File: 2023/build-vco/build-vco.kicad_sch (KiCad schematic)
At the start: 1 part, among them M27 NMOS_OR1

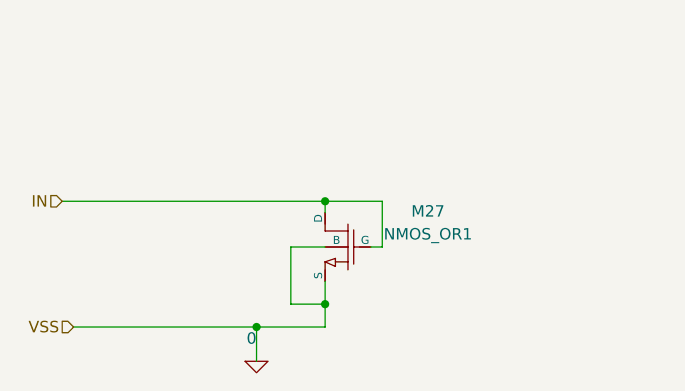
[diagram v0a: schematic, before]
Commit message: PMOS x1 NMOS x 2 まで成長させた。
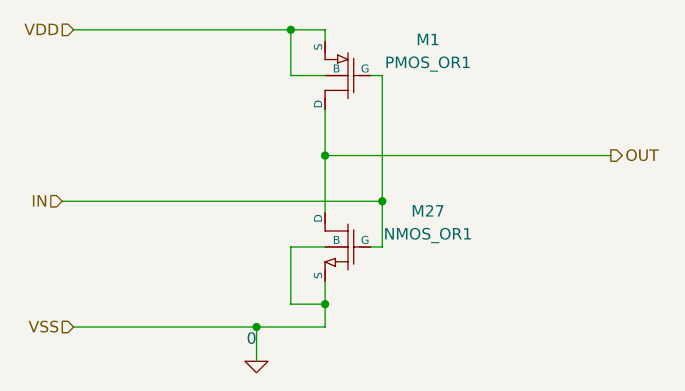
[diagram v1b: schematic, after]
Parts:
- added M1: PMOS_OR1, symbol OR1Symbols:PMOS_OR1
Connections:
- net IN: now also M1.2 (G); no longer M27.1 (D)
- new net OUT: M1.1 (D), M27.1 (D)
- new net VDD: M1.3 (S), M1.4 (B)
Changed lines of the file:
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@@
 (kicad_sch (version 20230121) (generator eeschema)
   (paper "A4")
-  (junction (at 132.08 73.66) (diameter 0) (color 0 0 0 0)
+  (junction (at 132.08 68.58) (diameter 0) (color 0 0 0 0)
+  )
+  (junction (at 138.43 73.66) (diameter 0) (color 0 0 0 0)
   )
   (junction (at 132.08 85.09) (diameter 0) (color 0 0 0 0)
   )
+  (junction (at 128.27 54.61) (diameter 0) (color 0 0 0 0)
+  )
   (junction (at 124.46 87.63) (diameter 0) (color 0 0 0 0)
   )
+  (wire (pts (xy 104.14 54.61) (xy 128.27 54.61))
+    (stroke (width 0) (type default))
+  )
+  (wire (pts (xy 132.08 54.61) (xy 132.08 55.88))
+    (stroke (width 0) (type default))
+  )
   (wire (pts (xy 104.14 87.63) (xy 124.46 87.63))
     (stroke (width 0) (type default))
   )
-  (wire (pts (xy 102.87 73.66) (xy 132.08 73.66))
-    (stroke (width 0) (type default))
-  )
-  (wire (pts (xy 132.08 73.66) (xy 132.08 74.93))
+  (wire (pts (xy 102.87 73.66) (xy 138.43 73.66))
+    (stroke (width 0) (type default))
+  )
+  (wire (pts (xy 137.16 59.69) (xy 138.43 59.69))
     (stroke (width 0) (type default))
   )
@@
     (stroke (width 0) (type default))
   )
-  (wire (pts (xy 132.08 73.66) (xy 138.43 73.66))
-    (stroke (width 0) (type default))
-  )
   (wire (pts (xy 124.46 87.63) (xy 124.46 91.44))
     (stroke (width 0) (type default))
@@
     (stroke (width 0) (type default))
   )
+  (wire (pts (xy 138.43 59.69) (xy 138.43 73.66))
+    (stroke (width 0) (type default))
+  )
+  (wire (pts (xy 132.08 68.58) (xy 163.83 68.58))
+    (stroke (width 0) (type default))
+  )
   (wire (pts (xy 128.27 78.74) (xy 128.27 85.09))
     (stroke (width 0) (type default))
@@
     (stroke (width 0) (type default))
   )
+  (wire (pts (xy 128.27 59.69) (xy 128.27 54.61))
+    (stroke (width 0) (type default))
+  )
+  (wire (pts (xy 132.08 59.69) (xy 128.27 59.69))
+    (stroke (width 0) (type default))
+  )
+  (wire (pts (xy 128.27 54.61) (xy 132.08 54.61))
+    (stroke (width 0) (type default))
+  )
   (wire (pts (xy 132.08 82.55) (xy 132.08 85.09))
     (stroke (width 0) (type default))
@@
   (wire (pts (xy 132.08 85.09) (xy 132.08 87.63))
     (stroke (width 0) (type default))
+  )
+  (wire (pts (xy 132.08 68.58) (xy 132.08 74.93))
+    (stroke (width 0) (type default))
+  )
+  (wire (pts (xy 132.08 63.5) (xy 132.08 68.58))
+    (stroke (width 0) (type default))
+  )
+  (hierarchical_label "VDD" (shape input) (at 104.14 54.61 180) (fields_autoplaced)
+    (effects (font (size 1.27 1.27)) (justify right))
   )
   (hierarchical_label "VSS" (shape input) (at 104.14 87.63 180) (fields_autoplaced)
     (effects (font (size 1.27 1.27)) (justify right))
+  )
+  (hierarchical_label "OUT" (shape output) (at 163.83 68.58 0) (fields_autoplaced)
+    (effects (font (size 1.27 1.27)) (justify left))
   )
   (hierarchical_label "IN" (shape input) (at 102.87 73.66 180) (fields_autoplaced)
@@
     )
   )
+  (symbol (lib_id "OR1Symbols:PMOS_OR1") (at 137.16 59.69 0) (mirror y) (unit 1)
+    (in_bom yes) (on_board yes) (dnp no) (fields_autoplaced)
+    (property "Reference" "M1" (at 143.51 55.7277 0)
+      (effects (font (size 1.27 1.27)))
+    )
+    (property "Value" "PMOS_OR1" (at 143.51 58.2677 0)
+      (effects (font (size 1.27 1.27)))
+    )
+    (property "Footprint" "" (at 137.16 59.69 0)
+      (effects (font (size 1.27 1.27)) hide)
+    )
+    (property "Datasheet" "" (at 137.16 59.69 0)
+      (effects (font (size 1.27 1.27)) hide)
+    )
+    (property "Sim.Pins" "1=1 2=2 3=3 4=4" (at 137.16 59.69 0)
+      (effects (font (size 1.27 1.27)) hide)
+    )
+    (property "Sim.Device" "SPICE" (at 128.27 64.77 0)
+      (effects (font (size 1.27 1.27)) (justify left) hide)
+    )
+    (property "Sim.Params" "type=\"M\" model=\"PMOS_OR1 l=1u w=6u\" lib=\"\"" (at 137.16 59.69 0)
+      (effects (font (size 1.27 1.27)) hide)
+    )
+    (pin "1")
+    (pin "2")
+    (pin "3")
+    (pin "4")
+    (instances
+      (project "build-vco"
+        (path "/178e7a69-f569-4b69-ab89-e6b9cdb6309f"
+          (reference "M1") (unit 1)
+        )
+      )
+    )
+  )
   (symbol (lib_id "OR1Symbols:0") (at 124.46 91.44 0) (unit 1)
     (in_bom yes) (on_board yes) (dnp no) (fields_autoplaced)
@@
           (reference "#GND02") (unit 1)
         )
+      )
+      (project "build-vco"
+        (path "/178e7a69-f569-4b69-ab89-e6b9cdb6309f"
+          (reference "#GND02") (unit 1)
+        )

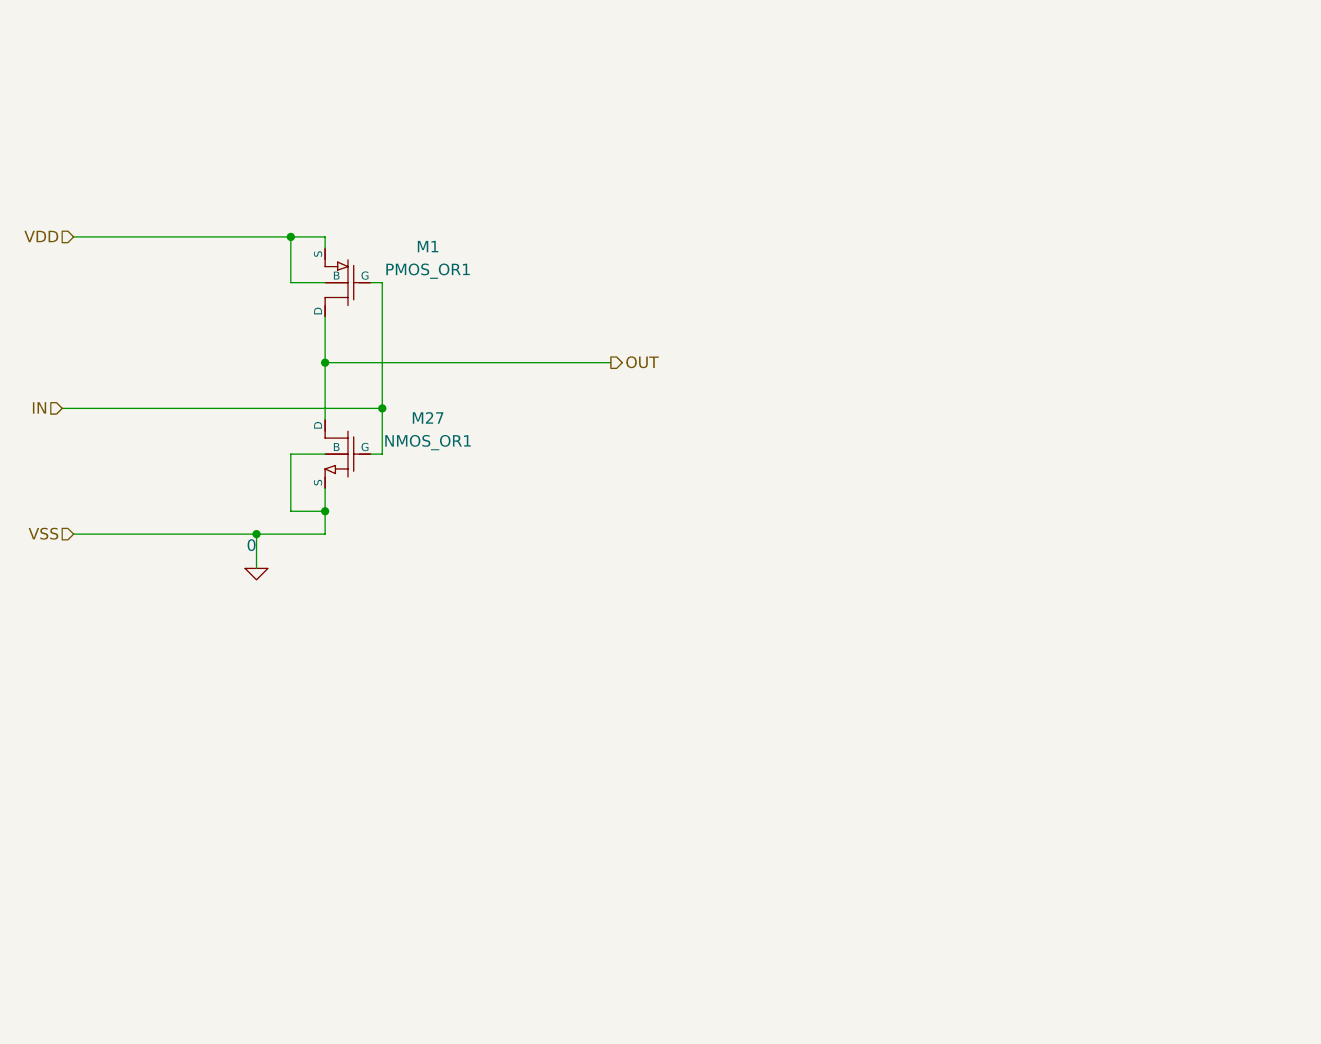
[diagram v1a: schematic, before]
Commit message: PMOS x 1, NMOS x1 に後退。しかし LVS は通る。
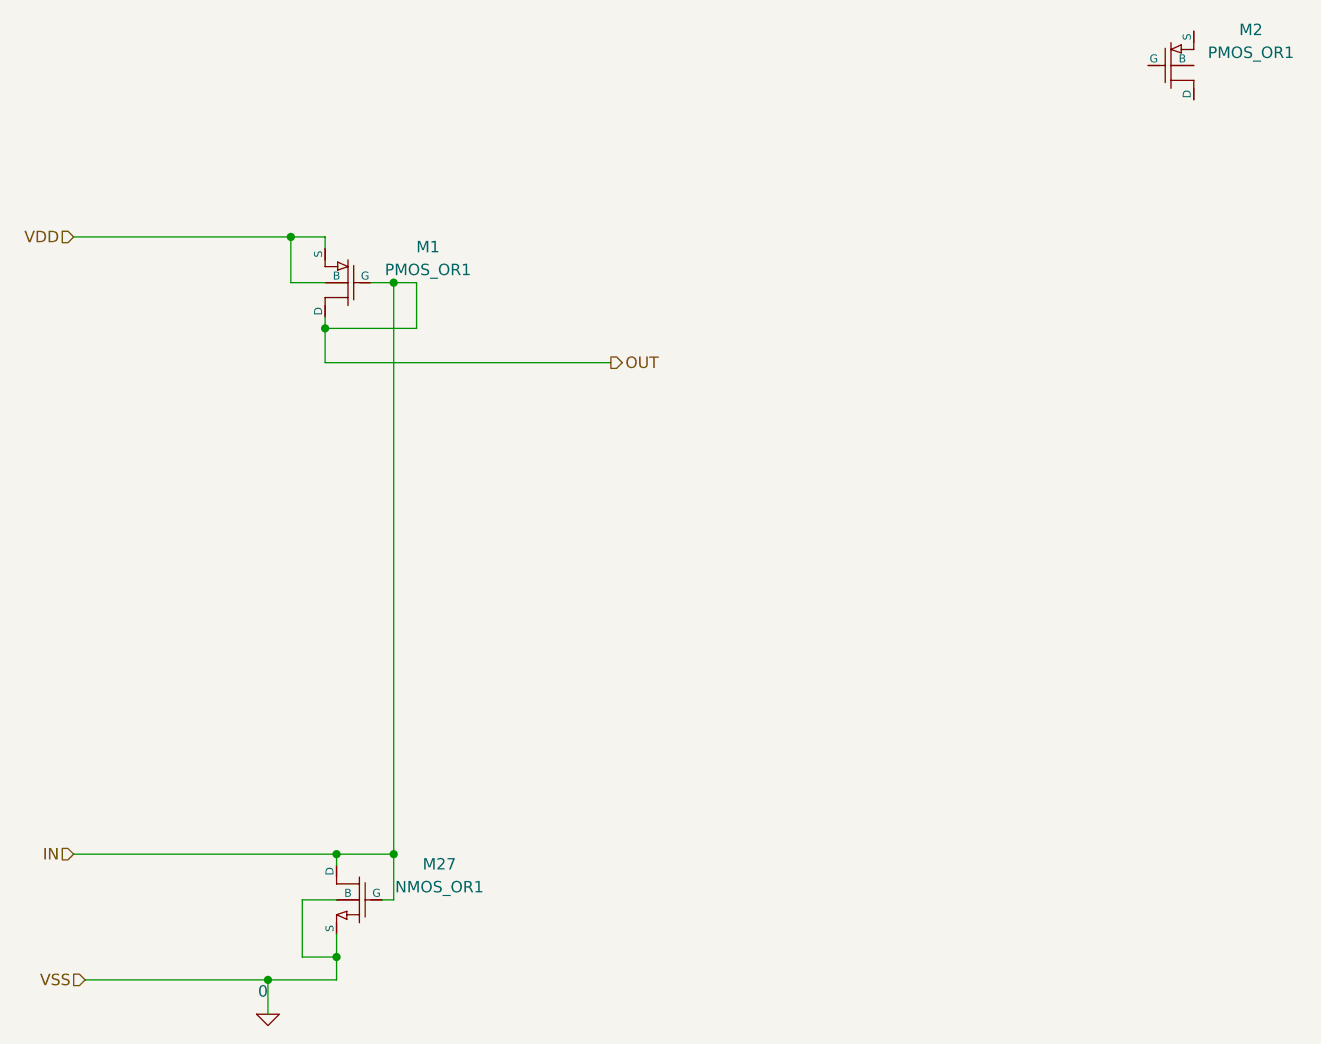
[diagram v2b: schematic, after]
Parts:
- added M2: PMOS_OR1, symbol OR1Symbols:PMOS_OR1
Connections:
- net OUT is gone; now on net IN: M1.1 (D), M27.1 (D)
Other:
- moved on the sheet: M27
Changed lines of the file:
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@@
 (kicad_sch (version 20230121) (generator eeschema)
   (paper "A4")
-  (junction (at 132.08 68.58) (diameter 0) (color 0 0 0 0)
-  )
-  (junction (at 138.43 73.66) (diameter 0) (color 0 0 0 0)
-  )
-  (junction (at 132.08 85.09) (diameter 0) (color 0 0 0 0)
+  (junction (at 133.35 123.19) (diameter 0) (color 0 0 0 0)
+  )
+  (junction (at 139.7 59.69) (diameter 0) (color 0 0 0 0)
+  )
+  (junction (at 139.7 123.19) (diameter 0) (color 0 0 0 0)
+  )
+  (junction (at 132.08 64.77) (diameter 0) (color 0 0 0 0)
+  )
+  (junction (at 133.35 134.62) (diameter 0) (color 0 0 0 0)
   )
   (junction (at 128.27 54.61) (diameter 0) (color 0 0 0 0)
   )
-  (junction (at 124.46 87.63) (diameter 0) (color 0 0 0 0)
+  (junction (at 125.73 137.16) (diameter 0) (color 0 0 0 0)
   )
   (wire (pts (xy 104.14 54.61) (xy 128.27 54.61))
@@
     (stroke (width 0) (type default))
   )
-  (wire (pts (xy 104.14 87.63) (xy 124.46 87.63))
-    (stroke (width 0) (type default))
-  )
-  (wire (pts (xy 102.87 73.66) (xy 138.43 73.66))
-    (stroke (width 0) (type default))
-  )
-  (wire (pts (xy 137.16 59.69) (xy 138.43 59.69))
-    (stroke (width 0) (type default))
-  )
-  (wire (pts (xy 138.43 73.66) (xy 138.43 78.74))
-    (stroke (width 0) (type default))
-  )
-  (wire (pts (xy 124.46 87.63) (xy 124.46 91.44))
-    (stroke (width 0) (type default))
-  )
-  (wire (pts (xy 132.08 78.74) (xy 128.27 78.74))
-    (stroke (width 0) (type default))
-  )
-  (wire (pts (xy 138.43 59.69) (xy 138.43 73.66))
+  (wire (pts (xy 105.41 137.16) (xy 125.73 137.16))
+    (stroke (width 0) (type default))
+  )
+  (wire (pts (xy 104.14 123.19) (xy 133.35 123.19))
+    (stroke (width 0) (type default))
+  )
+  (wire (pts (xy 139.7 123.19) (xy 139.7 128.27))
+    (stroke (width 0) (type default))
+  )
+  (wire (pts (xy 133.35 123.19) (xy 133.35 124.46))
+    (stroke (width 0) (type default))
+  )
+  (wire (pts (xy 125.73 137.16) (xy 125.73 140.97))
+    (stroke (width 0) (type default))
+  )
+  (wire (pts (xy 133.35 128.27) (xy 129.54 128.27))
+    (stroke (width 0) (type default))
+  )
+  (wire (pts (xy 139.7 59.69) (xy 139.7 123.19))
+    (stroke (width 0) (type default))
+  )
+  (wire (pts (xy 142.24 64.77) (xy 132.08 64.77))
+    (stroke (width 0) (type default))
+  )
+  (wire (pts (xy 129.54 128.27) (xy 129.54 134.62))
+    (stroke (width 0) (type default))
+  )
+  (wire (pts (xy 125.73 137.16) (xy 133.35 137.16))
+    (stroke (width 0) (type default))
+  )
+  (wire (pts (xy 138.43 128.27) (xy 139.7 128.27))
+    (stroke (width 0) (type default))
+  )
+  (wire (pts (xy 129.54 134.62) (xy 133.35 134.62))
+    (stroke (width 0) (type default))
+  )
+  (wire (pts (xy 137.16 59.69) (xy 139.7 59.69))
+    (stroke (width 0) (type default))
+  )
+  (wire (pts (xy 132.08 64.77) (xy 132.08 68.58))
+    (stroke (width 0) (type default))
+  )
+  (wire (pts (xy 128.27 59.69) (xy 128.27 54.61))
+    (stroke (width 0) (type default))
+  )
+  (wire (pts (xy 132.08 59.69) (xy 128.27 59.69))
+    (stroke (width 0) (type default))
+  )
+  (wire (pts (xy 128.27 54.61) (xy 132.08 54.61))
+    (stroke (width 0) (type default))
+  )
+  (wire (pts (xy 133.35 132.08) (xy 133.35 134.62))
+    (stroke (width 0) (type default))
+  )
+  (wire (pts (xy 139.7 59.69) (xy 142.24 59.69))
+    (stroke (width 0) (type default))
+  )
+  (wire (pts (xy 142.24 59.69) (xy 142.24 64.77))
+    (stroke (width 0) (type default))
+  )
+  (wire (pts (xy 133.35 123.19) (xy 139.7 123.19))
+    (stroke (width 0) (type default))
+  )
+  (wire (pts (xy 133.35 134.62) (xy 133.35 137.16))
     (stroke (width 0) (type default))
   )
@@
     (stroke (width 0) (type default))
   )
-  (wire (pts (xy 128.27 78.74) (xy 128.27 85.09))
-    (stroke (width 0) (type default))
-  )
-  (wire (pts (xy 124.46 87.63) (xy 132.08 87.63))
-    (stroke (width 0) (type default))
-  )
-  (wire (pts (xy 137.16 78.74) (xy 138.43 78.74))
-    (stroke (width 0) (type default))
-  )
-  (wire (pts (xy 128.27 85.09) (xy 132.08 85.09))
-    (stroke (width 0) (type default))
-  )
-  (wire (pts (xy 128.27 59.69) (xy 128.27 54.61))
-    (stroke (width 0) (type default))
-  )
-  (wire (pts (xy 132.08 59.69) (xy 128.27 59.69))
-    (stroke (width 0) (type default))
-  )
-  (wire (pts (xy 128.27 54.61) (xy 132.08 54.61))
-    (stroke (width 0) (type default))
-  )
-  (wire (pts (xy 132.08 82.55) (xy 132.08 85.09))
-    (stroke (width 0) (type default))
-  )
-  (wire (pts (xy 132.08 85.09) (xy 132.08 87.63))
-    (stroke (width 0) (type default))
-  )
-  (wire (pts (xy 132.08 68.58) (xy 132.08 74.93))
-    (stroke (width 0) (type default))
-  )
-  (wire (pts (xy 132.08 63.5) (xy 132.08 68.58))
+  (wire (pts (xy 132.08 63.5) (xy 132.08 64.77))
     (stroke (width 0) (type default))
   )
@@
     (effects (font (size 1.27 1.27)) (justify right))
   )
-  (hierarchical_label "VSS" (shape input) (at 104.14 87.63 180) (fields_autoplaced)
+  (hierarchical_label "VSS" (shape input) (at 105.41 137.16 180) (fields_autoplaced)
     (effects (font (size 1.27 1.27)) (justify right))
   )
@@
     (effects (font (size 1.27 1.27)) (justify left))
   )
-  (hierarchical_label "IN" (shape input) (at 102.87 73.66 180) (fields_autoplaced)
+  (hierarchical_label "IN" (shape input) (at 104.14 123.19 180) (fields_autoplaced)
     (effects (font (size 1.27 1.27)) (justify right))
   )
-  (symbol (lib_id "OR1Symbols:NMOS_OR1") (at 137.16 78.74 0) (mirror y) (unit 1)
-    (in_bom yes) (on_board yes) (dnp no) (fields_autoplaced)
-    (property "Reference" "M27" (at 143.51 74.7777 0)
-      (effects (font (size 1.27 1.27)))
-    )
-    (property "Value" "NMOS_OR1" (at 143.51 77.3177 0)
-      (effects (font (size 1.27 1.27)))
-    )
-    (property "Footprint" "" (at 137.16 78.74 0)
-      (effects (font (size 1.27 1.27)) hide)
-    )
-    (property "Datasheet" "" (at 137.16 78.74 0)
-      (effects (font (size 1.27 1.27)) hide)
-    )
-    (property "Sim.Pins" "1=1 2=2 3=3 4=4" (at 137.16 78.74 0)
-      (effects (font (size 1.27 1.27)) hide)
-    )
-    (property "Sim.Device" "SPICE" (at 128.27 83.82 0)
+  (symbol (lib_id "OR1Symbols:NMOS_OR1") (at 138.43 128.27 0) (mirror y) (unit 1)
+    (in_bom yes) (on_board yes) (dnp no) (fields_autoplaced)
+    (property "Reference" "M27" (at 144.78 124.3077 0)
+      (effects (font (size 1.27 1.27)))
+    )
+    (property "Value" "NMOS_OR1" (at 144.78 126.8477 0)
+      (effects (font (size 1.27 1.27)))
+    )
+    (property "Footprint" "" (at 138.43 128.27 0)
+      (effects (font (size 1.27 1.27)) hide)
+    )
+    (property "Datasheet" "" (at 138.43 128.27 0)
+      (effects (font (size 1.27 1.27)) hide)
+    )
+    (property "Sim.Pins" "1=1 2=2 3=3 4=4" (at 138.43 128.27 0)
+      (effects (font (size 1.27 1.27)) hide)
+    )
+    (property "Sim.Device" "SPICE" (at 129.54 133.35 0)
       (effects (font (size 1.27 1.27)) (justify left) hide)
     )
-    (property "Sim.Params" "type=\"M\" model=\"NMOS_OR1 l=1u w=2u\" lib=\"\"" (at 137.16 78.74 0)
+    (property "Sim.Params" "type=\"M\" model=\"NMOS_OR1 l=1u w=2u\" lib=\"\"" (at 138.43 128.27 0)
       (effects (font (size 1.27 1.27)) hide)
     )
@@
     )
   )
+  (symbol (lib_id "OR1Symbols:PMOS_OR1") (at 223.52 35.56 0) (unit 1)
+    (in_bom yes) (on_board yes) (dnp no) (fields_autoplaced)
+    (property "Reference" "M2" (at 234.95 31.5977 0)
+      (effects (font (size 1.27 1.27)))
+    )
+    (property "Value" "PMOS_OR1" (at 234.95 34.1377 0)
+      (effects (font (size 1.27 1.27)))
+    )
+    (property "Footprint" "" (at 223.52 35.56 0)
+      (effects (font (size 1.27 1.27)) hide)
+    )
+    (property "Datasheet" "" (at 223.52 35.56 0)
+      (effects (font (size 1.27 1.27)) hide)
+    )
+    (property "Sim.Pins" "1=1 2=2 3=3 4=4" (at 223.52 35.56 0)
+      (effects (font (size 1.27 1.27)) hide)
+    )
+    (property "Sim.Device" "SPICE" (at 232.41 40.64 0)
+      (effects (font (size 1.27 1.27)) (justify left) hide)
+    )
+    (property "Sim.Params" "type=\"M\" model=\"PMOS_OR1 l=1u w=6u\" lib=\"\"" (at 223.52 35.56 0)
+      (effects (font (size 1.27 1.27)) hide)
+    )
+    (pin "1")
+    (pin "2")
+    (pin "3")
+    (pin "4")
+    (instances
+      (project "build-vco"
+        (path "/178e7a69-f569-4b69-ab89-e6b9cdb6309f"
+          (reference "M2") (unit 1)
+        )
+      )
+    )
+  )
   (symbol (lib_id "OR1Symbols:PMOS_OR1") (at 137.16 59.69 0) (mirror y) (unit 1)
     (in_bom yes) (on_board yes) (dnp no) (fields_autoplaced)
@@
     )
   )
-  (symbol (lib_id "OR1Symbols:0") (at 124.46 91.44 0) (unit 1)
-    (in_bom yes) (on_board yes) (dnp no) (fields_autoplaced)
-    (property "Reference" "#GND02" (at 124.46 93.98 0)
-      (effects (font (size 1.27 1.27)) hide)
-    )
-    (property "Value" "0" (at 124.46 88.9 0)
+  (symbol (lib_id "OR1Symbols:0") (at 125.73 140.97 0) (unit 1)
+    (in_bom yes) (on_board yes) (dnp no) (fields_autoplaced)
+    (property "Reference" "#GND02" (at 125.73 143.51 0)
+      (effects (font (size 1.27 1.27)) hide)
+    )
+    (property "Value" "0" (at 125.73 138.43 0)
       (effects (font (size 1.27 1.27)) (justify right))
     )
-    (property "Footprint" "" (at 128.27 91.44 0)
-      (effects (font (size 1.27 1.27)) hide)
-    )
-    (property "Datasheet" "" (at 128.27 91.44 0)
-      (effects (font (size 1.27 1.27)) hide)
-    )
+    (property "Footprint" "" (at 129.54 140.97 0)
+      (effects (font (size 1.27 1.27)) hide)
+    )
+    (property "Datasheet" "" (at 129.54 140.97 0)
+      (effects (font (size 1.27 1.27)) hide)
+    )
